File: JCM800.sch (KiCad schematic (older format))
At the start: 114 parts, among them U1 ECC83, U2 ECC83, U3 ECC83, U4 EL84, U5 EL84

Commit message: Tweaks
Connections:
- net BIAS1: now also R40.1; no longer R40.2
- net GNDS: now also R42.1; no longer R42.2
- net at BIAS_U4.1, BIAS_U5.1, C24.2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: now also R40.2; no longer R40.1
- net at BIAS_U4.3, BIAS_U5.3: now also R42.2; no longer R42.1
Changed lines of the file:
@@
 F 3 "~" H 13750 8900 50  0001 C CNN
 	1    13750 8900
-	1    0    0    -1
+	-1   0    0    1
 $EndComp
 Wire Wire Line
@@
 Wire Wire Line
 	12450 7700 13000 7700
-$Comp
-L Device:R R41
-U 1 1 5E0B73F7
-P 13900 8000
-F 0 "R41" H 13970 8046 50  0000 L CNN
-F 1 "47K" H 13970 7955 50  0000 L CNN
-F 2 "Resistor_THT:R_Axial_DIN0207_L6.3mm_D2.5mm_P10.16mm_Horizontal" V 13830 8000 50  0001 C CNN
-F 3 "~" H 13900 8000 50  0001 C CNN
-	1    13900 8000
-	1    0    0    -1
-$EndComp
-$Comp
-L Device:R R40
-U 1 1 5E0B6F27
-P 13000 8000
-F 0 "R40" H 13070 8046 50  0000 L CNN
-F 1 "47K" H 13070 7955 50  0000 L CNN
-F 2 "Resistor_THT:R_Axial_DIN0207_L6.3mm_D2.5mm_P10.16mm_Horizontal" V 12930 8000 50  0001 C CNN
-F 3 "~" H 13000 8000 50  0001 C CNN
-	1    13000 8000
-	1    0    0    -1
-$EndComp
 Text Label 7400 8150 0    50   ~ 0
 BIAS1
@@
 	1    0    0    1
 $EndComp
+$Comp
+L Device:R R41
+U 1 1 5E0B73F7
+P 13900 8000
+F 0 "R41" H 13970 8046 50  0000 L CNN
+F 1 "47K" H 13970 7955 50  0000 L CNN
+F 2 "Resistor_THT:R_Axial_DIN0207_L6.3mm_D2.5mm_P10.16mm_Horizontal" V 13830 8000 50  0001 C CNN
+F 3 "~" H 13900 8000 50  0001 C CNN
+	1    13900 8000
+	1    0    0    -1
+$EndComp
+$Comp
+L Device:R R40
+U 1 1 5E0B6F27
+P 13000 8000
+F 0 "R40" H 13070 8046 50  0000 L CNN
+F 1 "47K" H 13070 7955 50  0000 L CNN
+F 2 "Resistor_THT:R_Axial_DIN0207_L6.3mm_D2.5mm_P10.16mm_Horizontal" V 12930 8000 50  0001 C CNN
+F 3 "~" H 13000 8000 50  0001 C CNN
+	1    13000 8000
+	-1   0    0    1
+$EndComp
 $EndSCHEMATC

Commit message: Tubes up
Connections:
- net A: now also AB1.2 (Pin_2); no longer AB1.1 (Pin_1)
- net B: now also AB1.1 (Pin_1); no longer AB1.2 (Pin_2)
- net FIL: now also FIL1.2 (Pin_2); no longer FIL1.1 (Pin_1)
- net GNDS: now also FIL1.1 (Pin_1); no longer FIL1.2 (Pin_2)
- net OUT1: now also OUT1.2 (Pin_2); no longer OUT1.1 (Pin_1)
- net OUT2: now also OUT1.1 (Pin_1); no longer OUT1.2 (Pin_2)
- net Tin1: now also AC1.1 (Pin_1); no longer AC1.2 (Pin_2)
- net Tin2: now also AC1.2 (Pin_2); no longer AC1.1 (Pin_1)
- net at R6.2, U1.8 (K): now also BOOST1.2 (Pin_2); no longer BOOST1.1 (Pin_1)
- net at C22.1: now also BOOST1.1 (Pin_1); no longer BOOST1.2 (Pin_2)

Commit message: Copper pour to the bottom layer
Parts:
- removed GND9: GND, Connector_PinHeader_2.54mm:PinHeader_1x01_P2.54mm_Vertical, symbol Connector:Conn_01x01_Male
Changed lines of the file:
@@
-$EndComp
-$Comp
-L Connector:Conn_01x01_Male GND9
-U 1 1 5DF1B207
-P 950 750
-F 0 "GND9" H 922 682 50  0000 R CNN
-F 1 "GND" H 922 773 50  0000 R CNN
-F 2 "Connector_PinHeader_2.54mm:PinHeader_1x01_P2.54mm_Vertical" H 950 750 50  0001 C CNN
-F 3 "~" H 950 750 50  0001 C CNN
-	1    950  750
-	1    0    0    -1
-$EndComp
-Wire Wire Line
-	1150 750  1350 750
-$Comp
-L power:GNDS #PWR0128
-U 1 1 5DF1B214
-P 1350 750
-F 0 "#PWR0128" H 1350 500 50  0001 C CNN
-F 1 "GNDS" H 1355 577 50  0000 C CNN
-F 2 "" H 1350 750 50  0001 C CNN
-F 3 "" H 1350 750 50  0001 C CNN
-	1    1350 750
-	1    0    0    -1
 $EndComp
 $Comp

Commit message: 6.3V Push-Pull version
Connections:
- net FIL: now also U1.5 (F1), U2.5 (F1), U3.5 (F1)
- net GNDS: now also U1.9 (F2), U2.9 (F2), U3.9 (F2); no longer U1.5 (F1), U2.5 (F1), U3.5 (F1)
- no-connect marks 8 -> 5
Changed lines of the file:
@@
 $EndComp
 Wire Wire Line
-	10750 2100 11550 2100
-Wire Wire Line
-	10950 1800 10950 2900
-Connection ~ 10950 2900
-Wire Wire Line
-	10950 2900 11750 2900
-Wire Wire Line
-	11750 1800 11750 2900
-NoConn ~ 11650 1800
-NoConn ~ 10850 1800
+	10750 2100 10950 2100
 Text Label 12350 4600 0    50   ~ 0
 TO_PA
@@
 Connection ~ 10450 2900
 Wire Wire Line
-	10450 2900 10950 2900
-Wire Wire Line
 	9650 2550 10050 2550
 Text Label 11200 7700 0    50   ~ 0
@@
 $EndComp
 Wire Wire Line
-	12600 2900 14300 2900
-NoConn ~ 12500 1800
-Wire Wire Line
-	12400 2100 13250 2100
+	12400 2100 12600 2100
 Wire Wire Line
 	12400 1800 12400 2100
-Wire Wire Line
-	12600 1800 12600 2900
-Connection ~ 12600 2900
-Connection ~ 11750 2900
-Wire Wire Line
-	11750 2900 12600 2900
 Connection ~ 12400 2100
 Connection ~ 11550 2100
 Wire Wire Line
-	11550 2100 12400 2100
+	11550 2100 11750 2100
 $Comp
 L Valve:ECC83 U3
@@
 	1    0    0    -1
 $EndComp
+Wire Wire Line
+	10450 2900 10850 2900
+Wire Wire Line
+	10950 1800 10950 2100
+Connection ~ 10950 2100
+Wire Wire Line
+	10950 2100 11550 2100
+Wire Wire Line
+	11750 1800 11750 2100
+Connection ~ 11750 2100
+Wire Wire Line
+	11750 2100 12400 2100
+Wire Wire Line
+	12600 1800 12600 2100
+Connection ~ 12600 2100
+Wire Wire Line
+	12600 2100 13250 2100
+Wire Wire Line
+	12500 1800 12500 2900
+Connection ~ 12500 2900
+Wire Wire Line
+	12500 2900 14300 2900
+Wire Wire Line
+	11650 1800 11650 2900
+Connection ~ 11650 2900
+Wire Wire Line
+	11650 2900 12500 2900
+Wire Wire Line
+	10850 1800 10850 2900
+Connection ~ 10850 2900
+Wire Wire Line
+	10850 2900 11650 2900
 $EndSCHEMATC

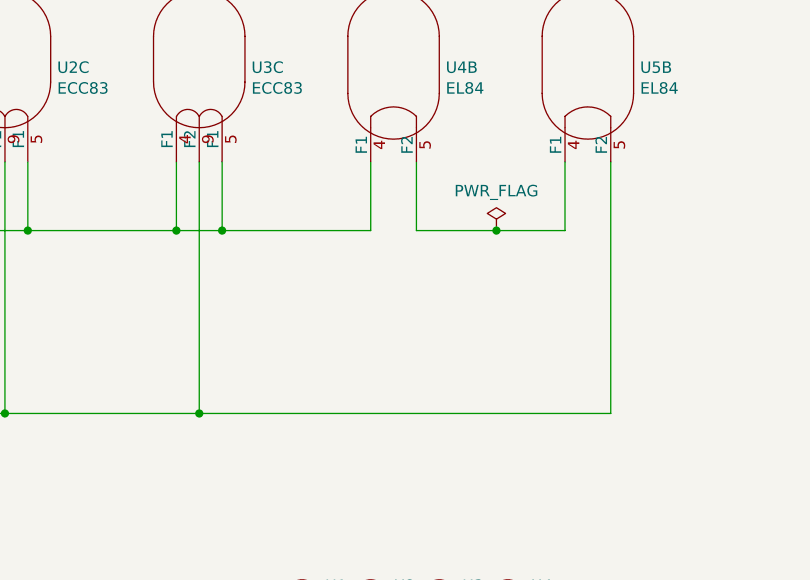
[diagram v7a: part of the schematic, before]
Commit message: EL84 filament wiring fixed
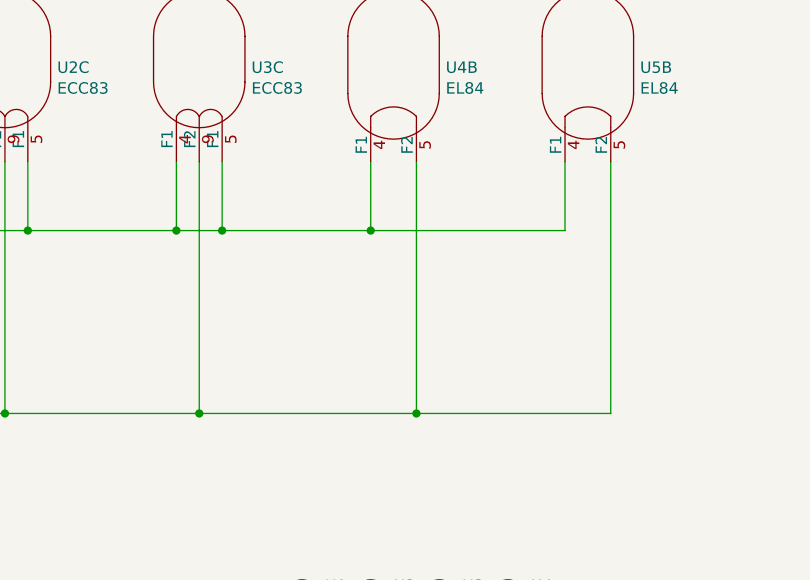
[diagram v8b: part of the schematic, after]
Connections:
- net FIL: now also U5.4 (F1)
- net GNDS: now also U4.5 (F2)
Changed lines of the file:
@@
 	14300 1800 14300 2900
 Wire Wire Line
-	13450 2100 13800 2100
-Wire Wire Line
 	14100 2100 14100 1800
-Wire Wire Line
-	13450 1800 13450 2100
-$Comp
-L power:PWR_FLAG #FLG0106
-U 1 1 5DEB167B
-P 13800 2100
-F 0 "#FLG0106" H 13800 2175 50  0001 C CNN
-F 1 "PWR_FLAG" H 13800 2273 50  0000 C CNN
-F 2 "" H 13800 2100 50  0001 C CNN
-F 3 "~" H 13800 2100 50  0001 C CNN
-	1    13800 2100
-	1    0    0    -1
-$EndComp
-Connection ~ 13800 2100
-Wire Wire Line
-	13800 2100 14100 2100
 $Comp
 L Mechanical:MountingHole H8
@@
 Connection ~ 12500 2900
 Wire Wire Line
-	12500 2900 14300 2900
+	12500 2900 13450 2900
 Wire Wire Line
 	11650 1800 11650 2900
@@
 Wire Wire Line
 	10850 2900 11650 2900
+Wire Wire Line
+	13450 1800 13450 2900
+Connection ~ 13450 2900
+Wire Wire Line
+	13450 2900 14300 2900
+Wire Wire Line
+	14100 2100 13250 2100
+Connection ~ 13250 2100
 $EndSCHEMATC
